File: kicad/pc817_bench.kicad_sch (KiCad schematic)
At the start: 27 parts, among them J1 24V, e-stops, lidars, U1 PC817, U2 PC817, U3 PC817, U4 PC817

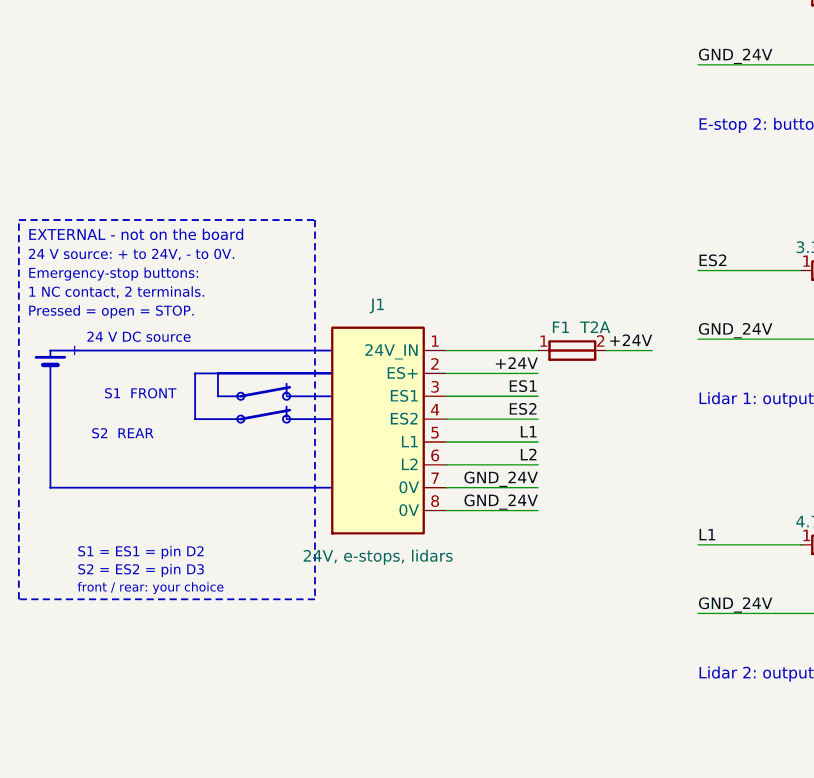
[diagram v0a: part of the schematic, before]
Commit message: Proto-shield: terminals as soldered (three 3-way 2.54 mm blocks at columns 8-10, 13-15, 18-20)
Supply on J1, e-stops on J2, lidars on J3. Fuse moved to row 5 (columns 8 and 6),
with a wire from the fused side to the ES+ screw. Schematic, plan and KiCad model
updated together; model matches the schematic.

Co-Authored-By: Claude Fable 5.1 <noreply@anthropic.com>
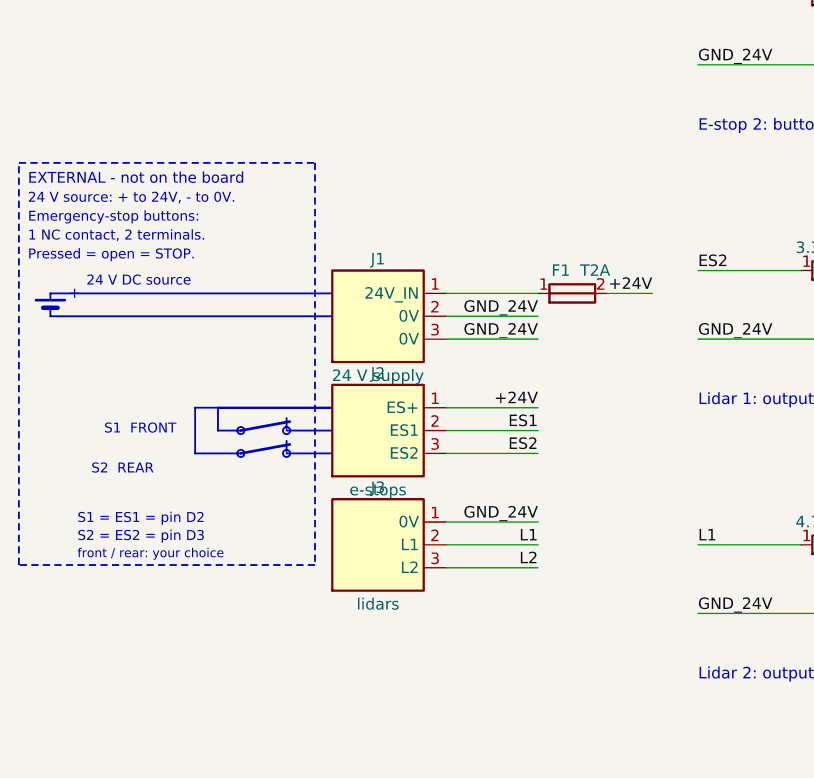
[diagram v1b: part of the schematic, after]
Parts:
- removed J1: 24V, e-stops, lidars, TerminalBlock_Phoenix:TerminalBlock_Phoenix_MKDS-1,5-8-5.08_1x08_P5.08mm_Horizontal, symbol bench:CONN8
- added J1: 24 V supply, TerminalBlock:TerminalBlock_Xinya_XY308-2.54-3P_1x03_P2.54mm_Horizontal, symbol bench:CONN3_1
- added J2: e-stops, TerminalBlock:TerminalBlock_Xinya_XY308-2.54-3P_1x03_P2.54mm_Horizontal, symbol bench:CONN3_2
- added J3: lidars, TerminalBlock:TerminalBlock_Xinya_XY308-2.54-3P_1x03_P2.54mm_Horizontal, symbol bench:CONN3_3
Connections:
- net +24V: now also J2.1 (ES+)
- net ES1: now also J2.2 (ES1)
- net ES2: now also J2.3 (ES2)
- net GND_24V: now also J1.2 (0V), J1.3 (0V), J3.1 (0V)
- net L1: now also J3.2 (L1)
- net L2: now also J3.3 (L2)
- net at F1.1: now also J1.1 (24V_IN)

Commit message: Proto-shield: fuse as built (flat in row 4, legs at columns 8 and 13)
It joins the 24V screw to the ES+ screw directly, so the extra wire is gone.

Co-Authored-By: Claude Fable 5.1 <noreply@anthropic.com>
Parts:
- F1: footprint Fuse:Fuse_Littelfuse_372_D8.50mm -> Resistor_THT:R_Axial_DIN0309_L9.0mm_D3.2mm_P12.70mm_Horizontal
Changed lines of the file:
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@@
     (property "Reference" "F1" (at 76.2 93.98 0) (effects (font (size 1.27 1.27))))
     (property "Value" "T2A" (at 80.01 93.98 0) (effects (font (size 1.27 1.27))))
-    (property "Footprint" "Fuse:Fuse_Littelfuse_372_D8.50mm" (at 77.47 96.52 0) (effects (font (size 1.27 1.27)) hide))
+    (property "Footprint" "Resistor_THT:R_Axial_DIN0309_L9.0mm_D3.2mm_P12.70mm_Horizontal" (at 77.47 96.52 0) (effects (font (size 1.27 1.27)) hide))
     (property "Datasheet" "" (at 77.47 96.52 0) (effects (font (size 1.27 1.27)) hide))
     (pin "1") (pin "2")
